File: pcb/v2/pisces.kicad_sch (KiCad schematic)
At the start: 55 parts, among them J1 USB_B_Micro, J2 AudioJack4, SW1 SW_PUSH, SW10 SW_PUSH, SW11 SW_PUSH, SW12 SW_PUSH, SW13 SW_PUSH, SW14 SW_PUSH, SW15 SW_PUSH, SW16 SW_PUSH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

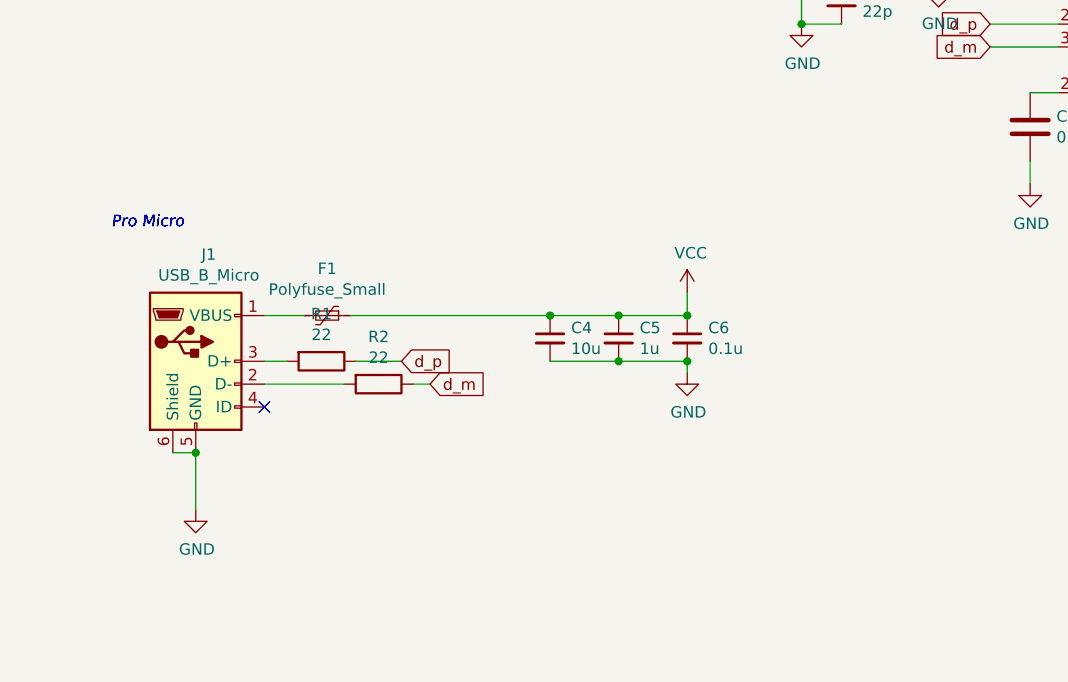
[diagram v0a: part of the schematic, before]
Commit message: Updated USB connector from Micro-B to USB-C (pisces ver 2.2) (#38)
* USB-C foot printをコピーしてきた

* USB-C version

* version should be 2.2

* Update pisces.kicad_pro

more exclusion
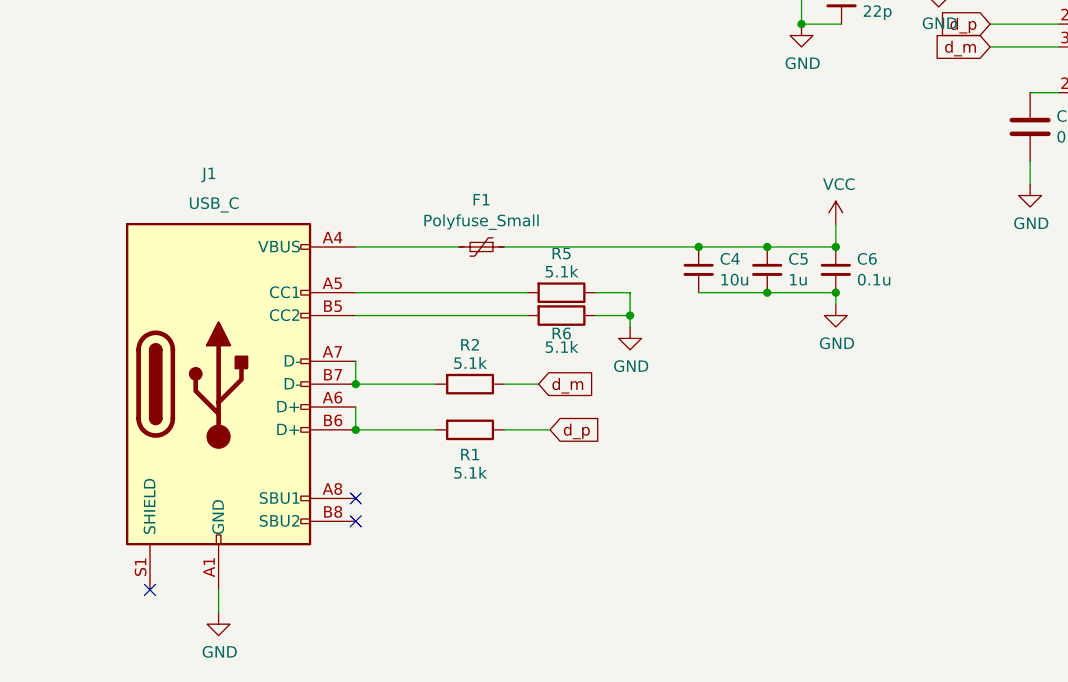
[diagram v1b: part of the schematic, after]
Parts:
- added R5, R6: 5.1k, Resistor_SMD:R_0402_1005Metric, symbol Device:R
- J1: value USB_B_Micro -> USB_C; footprint pisces_v2:HRS_ZX62R-B-5P -> pisces_v2:USB_C_Receptacle_XKB_U262-16XN-4BVC11; symbol Connector:USB_B_Micro -> Connector:USB_C_Receptacle_USB2.0_16P
- R1, R2: value 22 -> 5.1k
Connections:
- net GND: now also J1.A1 (GND), J1.A12 (GND), J1.B1 (GND), J1.B12 (GND), R5.1, R6.1; no longer J1.5 (GND), J1.6 (Shield)
- net at F1.2: now also J1.A4 (VBUS), J1.A9 (VBUS), J1.B4 (VBUS), J1.B9 (VBUS); no longer J1.1 (VBUS)
- net at R2.2: now also J1.A7 (D-), J1.B7 (D-); no longer J1.2 (D-)
- net at R1.2: now also J1.A6 (D+), J1.B6 (D+); no longer J1.3 (D+)
- new net: J1.A5 (CC1), R5.2
- new net: J1.B5 (CC2), R6.2
- no-connect marks 11 -> 13
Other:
- note removed: "Pro Micro"
- moved on the sheet: C4, C5, C6, F1, R1, R2
